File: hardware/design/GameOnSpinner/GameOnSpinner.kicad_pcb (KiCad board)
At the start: 2 copper layers, 10 parts, among them IC1 A1302KLHLT-T, IC2 A1302KLHLT-T, IC3 A1302KLHLT-T, IC4 A1302KLHLT-T, IC5 A1302KLHLT-T, IC6 A1302KLHLT-T, IC7 A1302KLHLT-T, IC8 A1302KLHLT-T, P1 CONN_01X15, P2 CONN_01X15

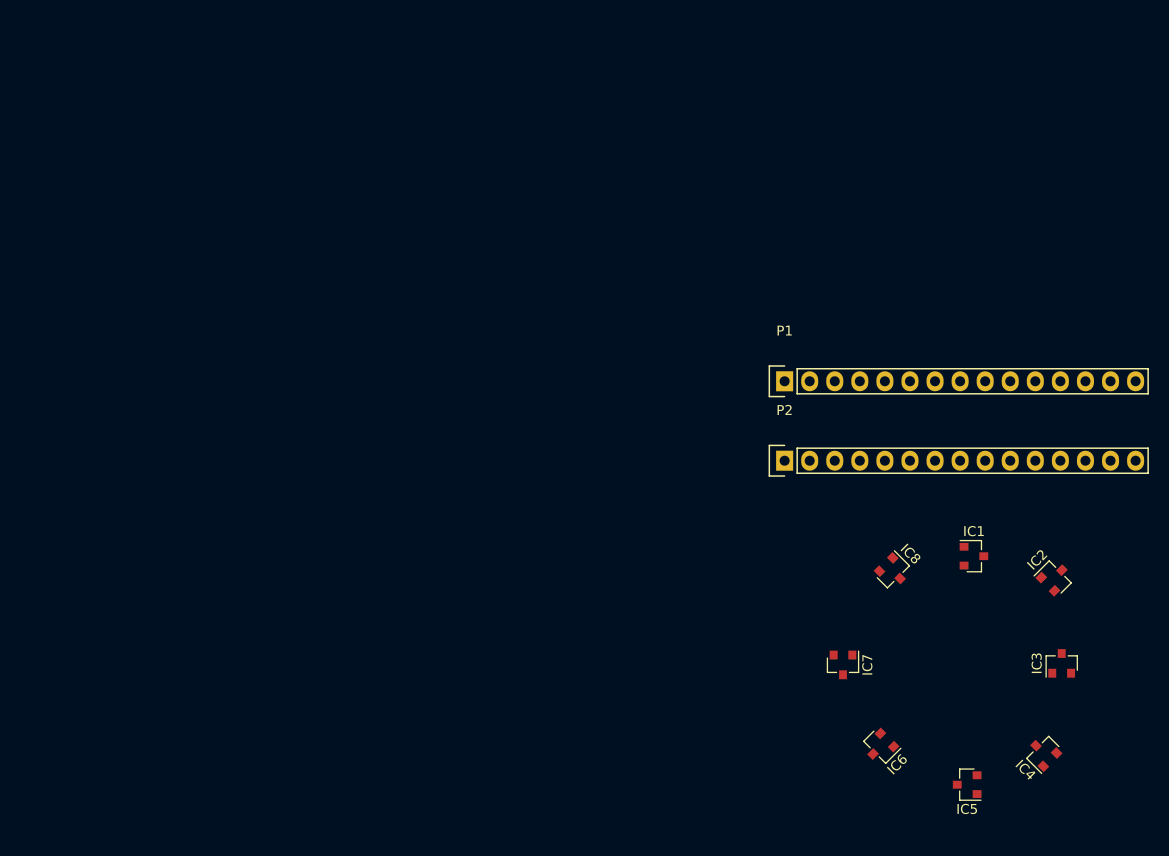
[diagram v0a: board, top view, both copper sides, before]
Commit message: Proper spacing for hall sensors.
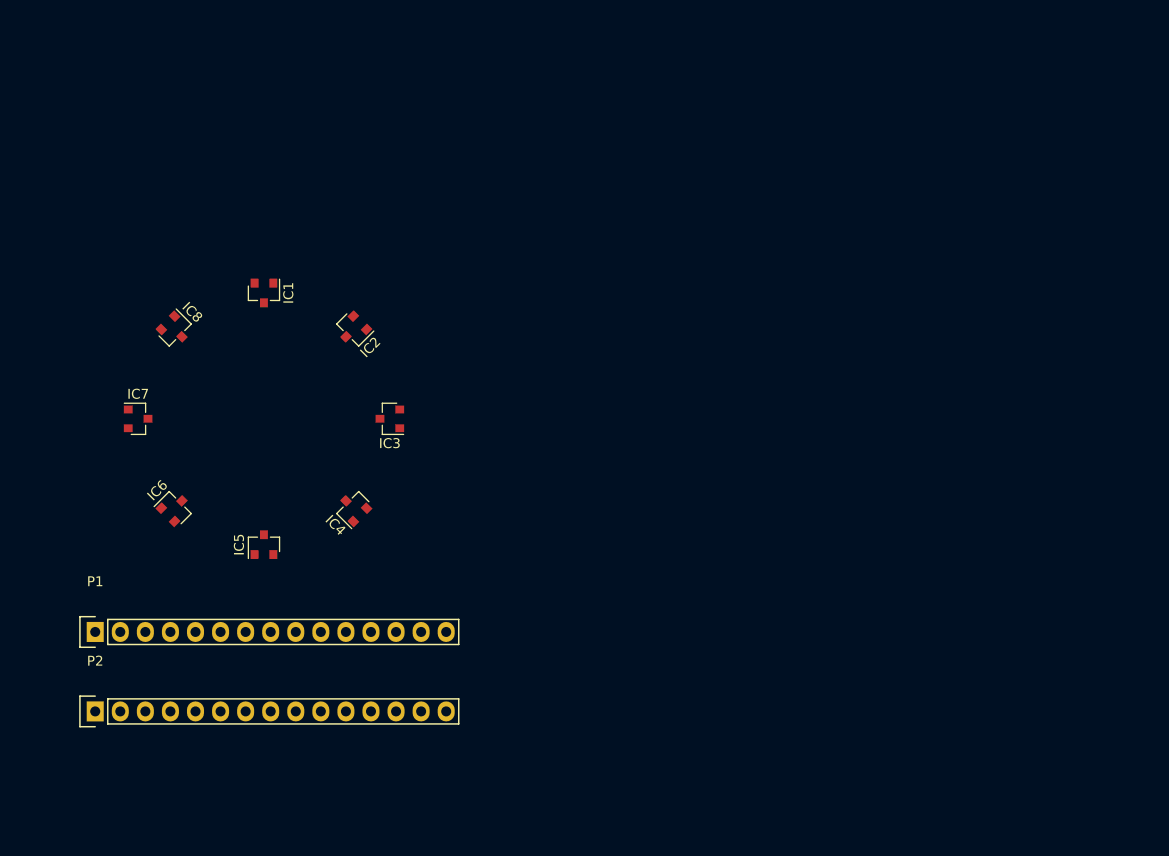
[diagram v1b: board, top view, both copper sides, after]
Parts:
- moved IC8 76.8 mm to (116.0, 103.7)
- moved IC1 76.7 mm to (125.0, 100.0), turned to 270 degrees
- moved IC7 75.6 mm to (112.2, 112.8), turned to 0 degrees
- moved IC6 75.4 mm to (116.0, 121.8), turned to 45 degrees
- moved IC2 75.4 mm to (134.0, 103.7), turned to 225 degrees
- moved IC5 75.3 mm to (125.0, 125.5), turned to 90 degrees
- moved P1 74.3 mm to (107.9, 134.3)
- moved P2 74.3 mm to (107.9, 142.4)
- moved IC4 74.2 mm to (134.0, 121.8)
- moved IC3 72.4 mm to (137.8, 112.8), turned to 180 degrees

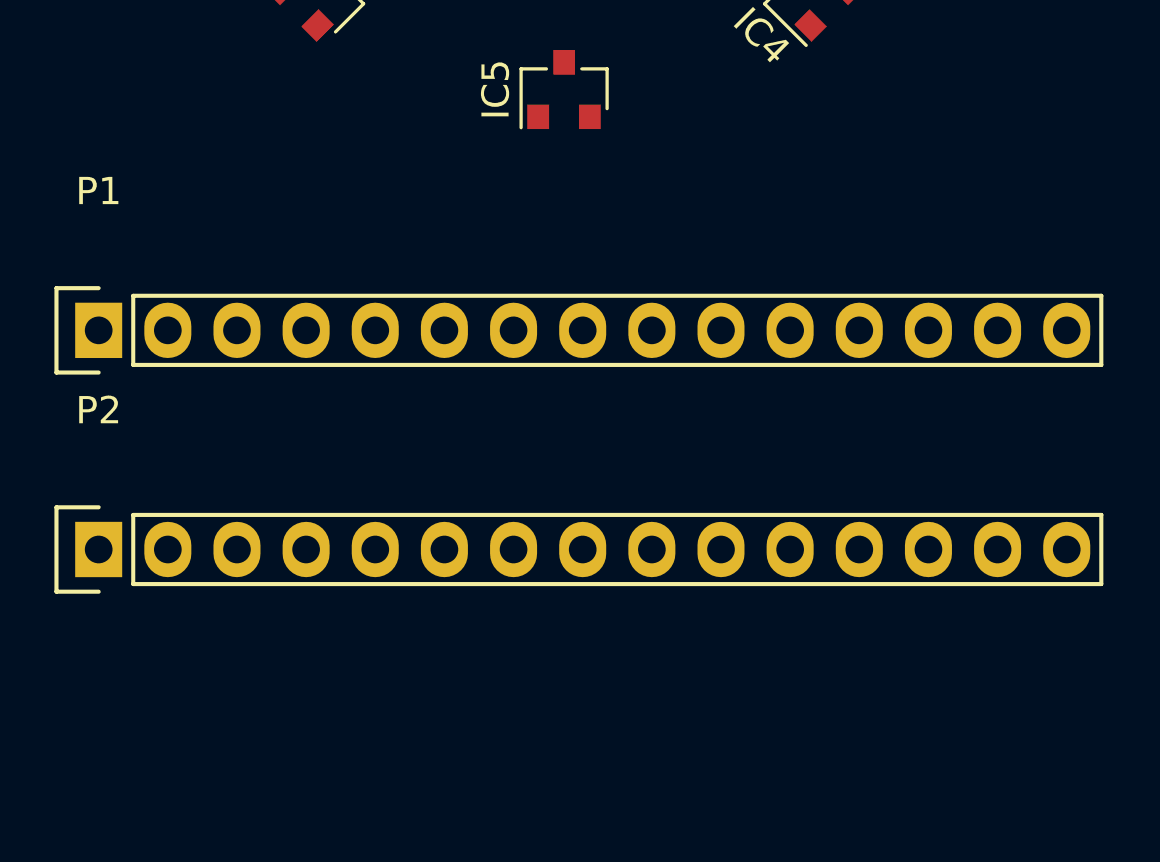
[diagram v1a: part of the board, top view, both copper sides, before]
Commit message: Position header strips for nano.
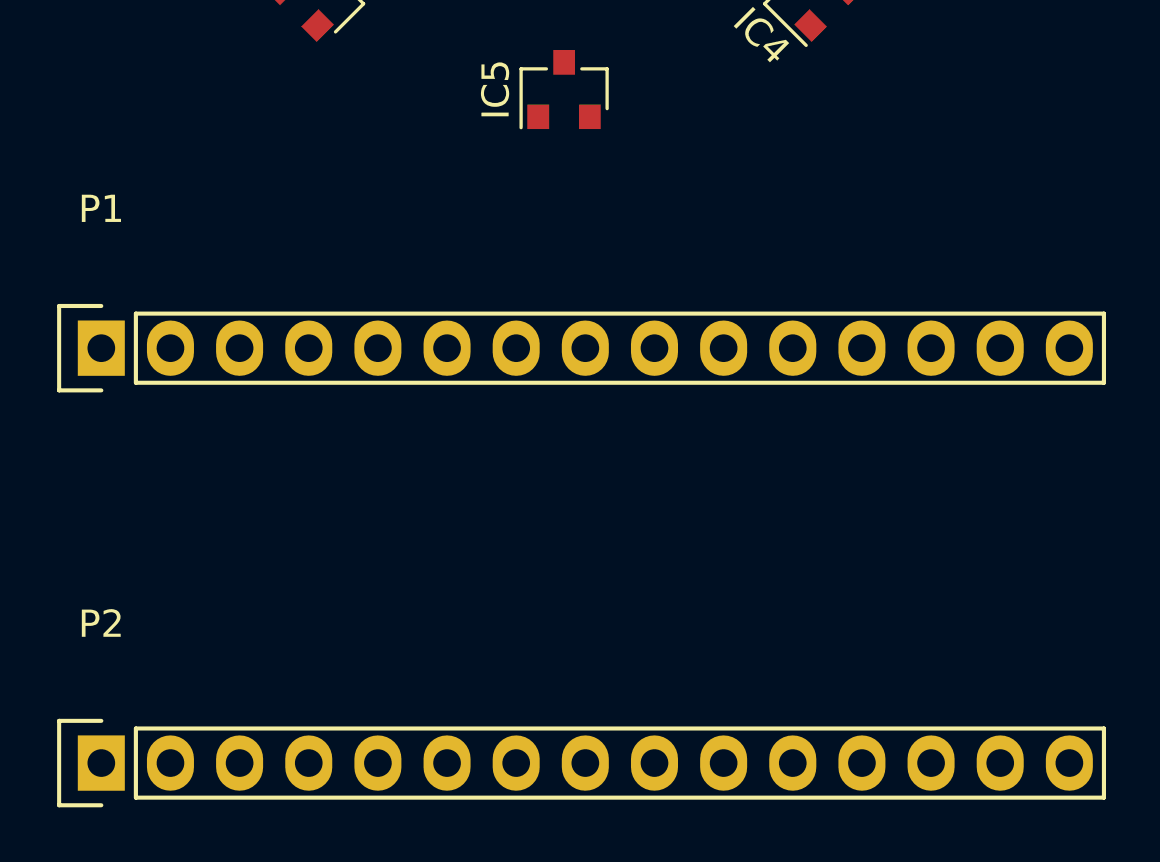
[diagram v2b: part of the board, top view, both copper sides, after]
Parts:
- moved P2 7.85 mm to (108.0, 150.2)
- moved P1 0.66 mm to (108.0, 135.0)
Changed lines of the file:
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@@
     (mod_text_size 1 1)
     (mod_text_width 0.15)
-    (pad_size 0.9 0.8)
-    (pad_drill 0)
+    (pad_size 1.7272 2.032)
+    (pad_drill 1.016)
     (pad_to_mask_clearance 0.2)
     (aux_axis_origin 0 0)
@@
   )
   (module Socket_Strips:Socket_Strip_Straight_1x15 (layer F.Cu)
-    (at 107.903333 134.345)
+    (at 108 135)
     (descr "Through hole socket strip")
     (tags "socket strip")
@@
   )
   (module Socket_Strips:Socket_Strip_Straight_1x15 (layer F.Cu)
-    (at 107.903333 142.395)
+    (at 108 150.24)
     (descr "Through hole socket strip")
     (tags "socket strip")

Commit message: Add outline.
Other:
- board outline added: 50.8 x 62.2 mm
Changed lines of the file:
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@@
     (area 172.72 102.87 215.328334 153.39)
     (thickness 1.6)
-    (drawings 0)
+    (drawings 5)
     (tracks 0)
     (zones 0)
@@
     )
   )
+  (gr_line (start 100.33 154.94) (end 101.6 154.94) (angle 90) (layer Edge.Cuts) (width 0.15))
+  (gr_line (start 100.33 92.71) (end 100.33 154.94) (angle 90) (layer Edge.Cuts) (width 0.15))
+  (gr_line (start 151.13 92.71) (end 100.33 92.71) (angle 90) (layer Edge.Cuts) (width 0.15))
+  (gr_line (start 151.13 154.94) (end 151.13 92.71) (angle 90) (layer Edge.Cuts) (width 0.15))
+  (gr_line (start 101.6 154.94) (end 151.13 154.94) (angle 90) (layer Edge.Cuts) (width 0.15))
 )

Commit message: Routing.
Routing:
- net Net-(IC1-Pad1): track 0.00 -> 115.1 mm, vias 0 -> 8
- net Net-(IC1-Pad3): track 0.00 -> 94.2 mm, vias 0 -> 8
- net Net-(IC1-Pad2): track 0.00 -> 58.4 mm
- net Net-(IC2-Pad2): track 0.00 -> 46.4 mm
- net Net-(IC8-Pad2): track 0.00 -> 38.4 mm
- net Net-(IC3-Pad2): track 0.00 -> 33.2 mm
- net Net-(IC7-Pad2): track 0.00 -> 24.2 mm
- net Net-(IC4-Pad2): track 0.00 -> 20.2 mm
- net Net-(IC6-Pad2): track 0.00 -> 13.8 mm
- net Net-(IC5-Pad2): track 0.00 -> 9.62 mm

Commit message: Add bluetooth board.
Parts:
- added P3: CONN_01X06, Socket_Strips:Socket_Strip_Straight_1x06, B.Cu at (139.5, 76.5)
- P1, P2: moved to B.Cu
- moved P1 34.3 mm to (142.3, 134.6), turned to 180 degrees
- moved P2 34.3 mm to (142.3, 149.8), turned to 180 degrees
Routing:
- net Net-(P2-Pad5): track 0.00 -> 156.1 mm
- net Net-(P2-Pad6): track 0.00 -> 94.1 mm
- net Net-(P2-Pad4): track 0.00 -> 74.4 mm
- net Net-(P1-Pad2): track 0.00 -> 51.6 mm
- net Net-(IC8-Pad2): track 38.4 -> 79.8 mm
- net Net-(IC7-Pad2): track 24.2 -> 59.4 mm
- net Net-(IC6-Pad2): track 13.8 -> 47.8 mm
- net Net-(IC1-Pad3): track 94.2 -> 116.7 mm, vias 8 -> 9
- net Net-(IC1-Pad1): track 115.1 -> 132.5 mm, vias 8 -> 9
- net Net-(IC1-Pad2): track 58.4 -> 43.7 mm
- net Net-(IC4-Pad2): track 20.2 -> 31.4 mm
- net Net-(IC3-Pad2): track 33.2 -> 39.2 mm
- net Net-(IC5-Pad2): track 9.62 -> 8.50 mm
- net Net-(IC2-Pad2): track 46.4 -> 47.3 mm
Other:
- board size 50.8 x 62.2 mm -> 50.8 x 82.5 mm
